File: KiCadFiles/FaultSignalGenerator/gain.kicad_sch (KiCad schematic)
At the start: 16 parts

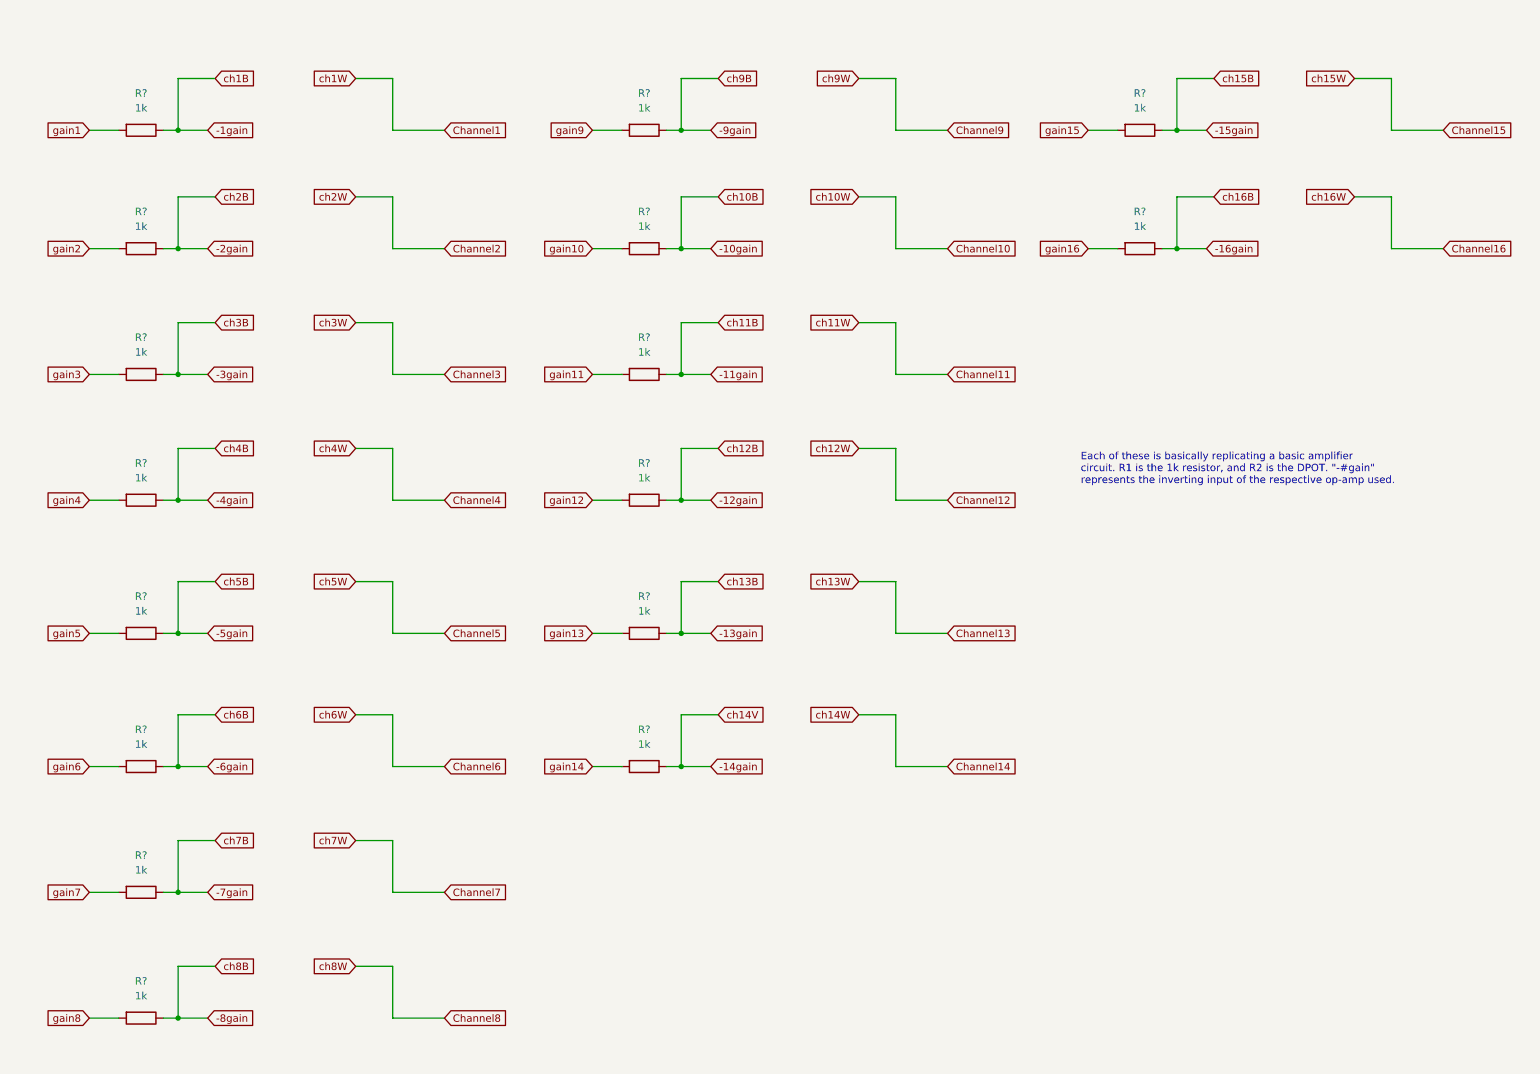
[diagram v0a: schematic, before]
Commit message: Finish schematic, start on PCB
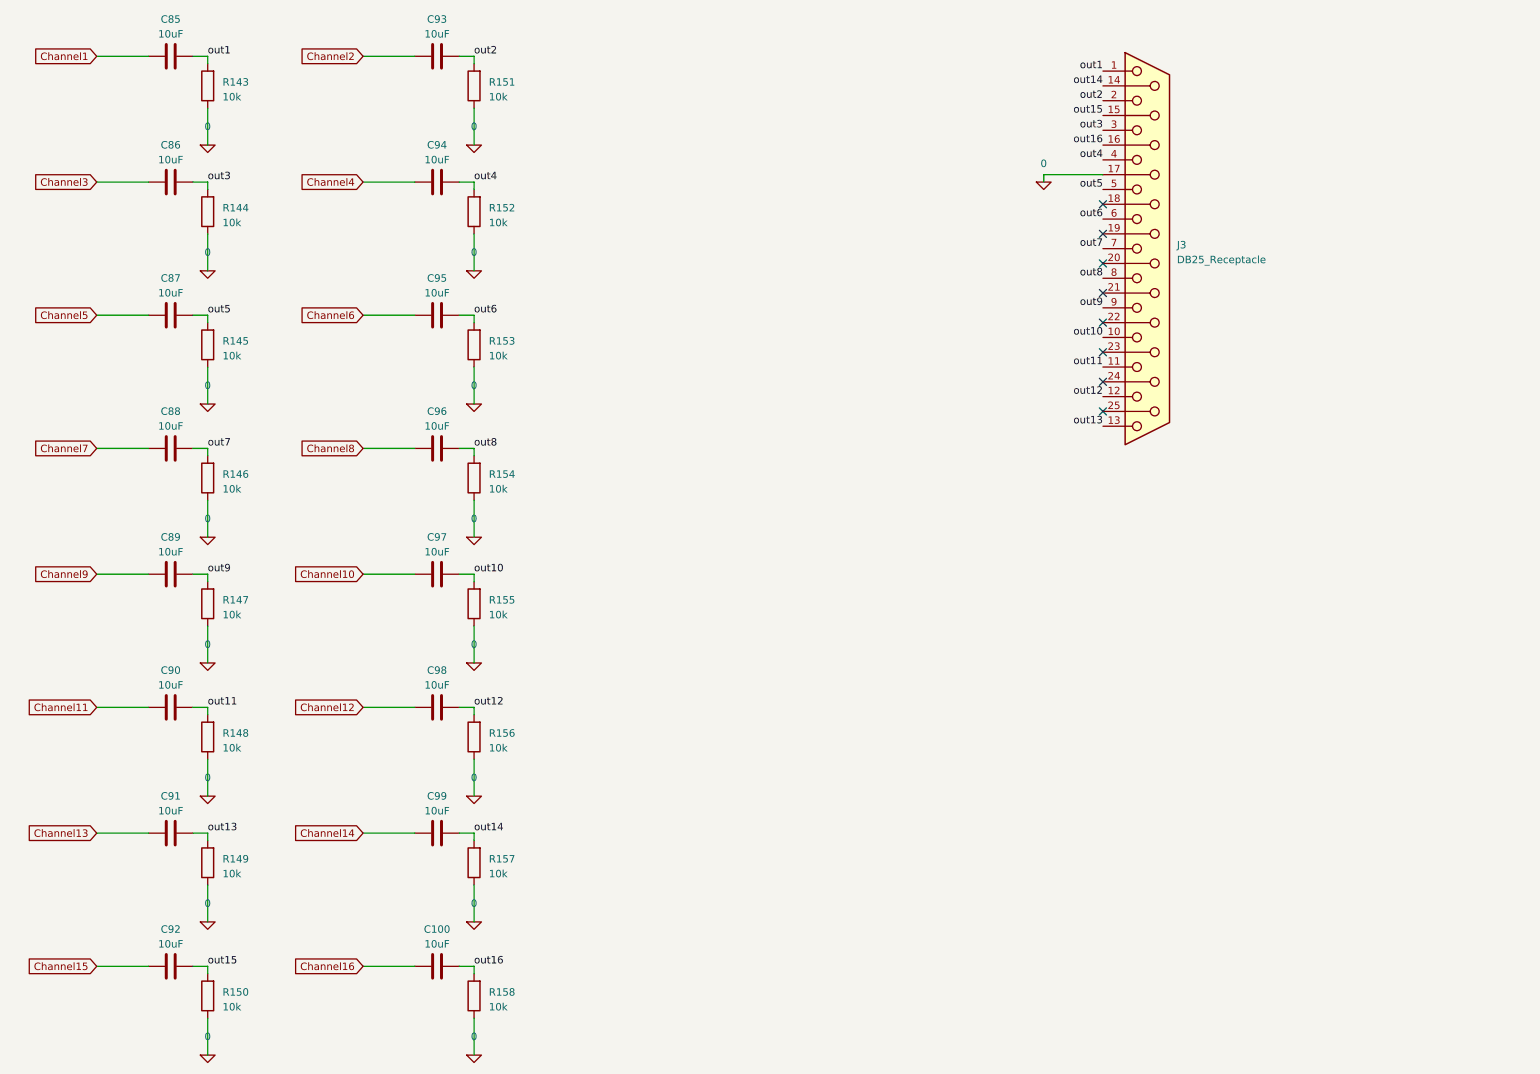
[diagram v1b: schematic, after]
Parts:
- removed R? (x16): 1k, Resistor_SMD:R_0603_1608Metric_Pad0.98x0.95mm_HandSolder, symbol Device:R
- added C100, C85, C86, C87, C88, C89, C90, C91, C92, C93, C94, C95, C96, C97, C98, C99: 10uF, Capacitor_SMD:C_1206_3216Metric_Pad1.33x1.80mm_HandSolder, symbol Device:C
- added J3: DB25_Receptacle, DSUB-25_Female_Horizontal_P2.77x2.54mm_EdgePinOffset9.40mm, symbol Connector:DB25_Receptacle
- added R143, R144, R145, R146, R147, R148, R149, R150, R151, R152, R153, R154, R155, R156, R157, R158: 10k, Resistor_SMD:R_1206_3216Metric, symbol Device:R
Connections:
- net Channel1: now also C85.1
- net Channel10: now also C97.1
- net Channel11: now also C90.1
- net Channel12: now also C98.1
- net Channel13: now also C91.1
- net Channel14: now also C99.1
- net Channel15: now also C92.1
- net Channel16: now also C100.1
- net Channel2: now also C93.1
- net Channel3: now also C86.1
- net Channel4: now also C94.1
- net Channel5: now also C87.1
- net Channel6: now also C95.1
- net Channel7: now also C88.1
- net Channel8: now also C96.1
- net Channel9: now also C89.1
- new net 0: J3.17 (P17), R143.1, R144.1, R145.1, R146.1, R147.1, R148.1, R149.1, R150.1, R151.1, R152.1, R153.1, R154.1, R155.1, R156.1, R157.1, R158.1
- new net out1: C85.2, J3.1, R143.2
- new net out10: C97.2, J3.10, R155.2
- new net out11: C90.2, J3.11, R148.2
- new net out12: C98.2, J3.12, R156.2
- new net out13: C91.2, J3.13, R149.2
- new net out14: C99.2, J3.14 (P14), R157.2
- new net out15: C92.2, J3.15 (P15), R150.2
- new net out16: C100.2, J3.16 (P16), R158.2
- new net out2: C93.2, J3.2, R151.2
- new net out3: C86.2, J3.3, R144.2
- new net out4: C94.2, J3.4, R152.2
- new net out5: C87.2, J3.5, R145.2
- new net out6: C95.2, J3.6, R153.2
- new net out7: C88.2, J3.7, R146.2
- new net out8: C96.2, J3.8, R154.2
- new net out9: C89.2, J3.9, R147.2
- no-connect marks 0 -> 8
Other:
- note removed: "Each of these is basically replicating a basic amplifier circuit. R1 is the 1k resistor, and R2 is the DPOT. "-#gain" represents the inverting input of the respective op-amp used."

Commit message: finish layout
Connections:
- net out1: now also J3.13; no longer J3.1
- net out10: now also J3.4; no longer J3.10
- net out11: now also J3.3; no longer J3.11
- net out12: now also J3.2; no longer J3.12
- net out13: now also J3.1; no longer J3.13
- net out14: now also J3.25 (P25); no longer J3.14 (P14)
- net out15: now also J3.24 (P24); no longer J3.15 (P15)
- net out16: now also J3.23 (P23); no longer J3.16 (P16)
- net out2: now also J3.12; no longer J3.2
- net out3: now also J3.11; no longer J3.3
- net out4: now also J3.10; no longer J3.4
- net out5: now also J3.9; no longer J3.5
- net out6: now also J3.8; no longer J3.6
- net out8: now also J3.6; no longer J3.8
- net out9: now also J3.5; no longer J3.9
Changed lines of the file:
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@@
     (stroke (width 0) (type default))
   )
-  (label "out12" (at 212.09 80.01 180) (fields_autoplaced)
+  (label "out12" (at 212.09 29.21 180) (fields_autoplaced)
     (effects (font (size 1.27 1.27)) (justify right bottom))
   )
-  (label "out10" (at 212.09 69.85 180) (fields_autoplaced)
+  (label "out10" (at 212.09 39.37 180) (fields_autoplaced)
     (effects (font (size 1.27 1.27)) (justify right bottom))
   )
@@
     (effects (font (size 1.27 1.27)) (justify left bottom))
   )
-  (label "out6" (at 212.09 49.53 180) (fields_autoplaced)
+  (label "out6" (at 212.09 59.69 180) (fields_autoplaced)
     (effects (font (size 1.27 1.27)) (justify right bottom))
   )
@@
     (effects (font (size 1.27 1.27)) (justify left bottom))
   )
-  (label "out15" (at 212.09 31.75 180) (fields_autoplaced)
+  (label "out15" (at 212.09 77.47 180) (fields_autoplaced)
     (effects (font (size 1.27 1.27)) (justify right bottom))
   )
@@
     (effects (font (size 1.27 1.27)) (justify left bottom))
   )
-  (label "out8" (at 212.09 59.69 180) (fields_autoplaced)
+  (label "out8" (at 212.09 49.53 180) (fields_autoplaced)
     (effects (font (size 1.27 1.27)) (justify right bottom))
   )
@@
     (effects (font (size 1.27 1.27)) (justify right bottom))
   )
-  (label "out1" (at 212.09 24.13 180) (fields_autoplaced)
+  (label "out1" (at 212.09 85.09 180) (fields_autoplaced)
     (effects (font (size 1.27 1.27)) (justify right bottom))
   )
@@
     (effects (font (size 1.27 1.27)) (justify left bottom))
   )
-  (label "out4" (at 212.09 39.37 180) (fields_autoplaced)
+  (label "out4" (at 212.09 69.85 180) (fields_autoplaced)
     (effects (font (size 1.27 1.27)) (justify right bottom))
   )
-  (label "out11" (at 212.09 74.93 180) (fields_autoplaced)
+  (label "out11" (at 212.09 34.29 180) (fields_autoplaced)
     (effects (font (size 1.27 1.27)) (justify right bottom))
   )
@@
     (effects (font (size 1.27 1.27)) (justify left bottom))
   )
-  (label "out5" (at 212.09 44.45 180) (fields_autoplaced)
+  (label "out5" (at 212.09 64.77 180) (fields_autoplaced)
     (effects (font (size 1.27 1.27)) (justify right bottom))
   )
-  (label "out16" (at 212.09 36.83 180) (fields_autoplaced)
+  (label "out16" (at 212.09 72.39 180) (fields_autoplaced)
     (effects (font (size 1.27 1.27)) (justify right bottom))
   )
@@
     (effects (font (size 1.27 1.27)) (justify left bottom))
   )
-  (label "out2" (at 212.09 29.21 180) (fields_autoplaced)
+  (label "out2" (at 212.09 80.01 180) (fields_autoplaced)
     (effects (font (size 1.27 1.27)) (justify right bottom))
   )
-  (label "out9" (at 212.09 64.77 180) (fields_autoplaced)
+  (label "out9" (at 212.09 44.45 180) (fields_autoplaced)
     (effects (font (size 1.27 1.27)) (justify right bottom))
   )
@@
     (effects (font (size 1.27 1.27)) (justify left bottom))
   )
-  (label "out14" (at 212.09 26.67 180) (fields_autoplaced)
+  (label "out14" (at 212.09 82.55 180) (fields_autoplaced)
     (effects (font (size 1.27 1.27)) (justify right bottom))
   )
@@
     (effects (font (size 1.27 1.27)) (justify left bottom))
   )
-  (label "out13" (at 212.09 85.09 180) (fields_autoplaced)
+  (label "out13" (at 212.09 24.13 180) (fields_autoplaced)
     (effects (font (size 1.27 1.27)) (justify right bottom))
   )
-  (label "out3" (at 212.09 34.29 180) (fields_autoplaced)
+  (label "out3" (at 212.09 74.93 180) (fields_autoplaced)
     (effects (font (size 1.27 1.27)) (justify right bottom))
   )
